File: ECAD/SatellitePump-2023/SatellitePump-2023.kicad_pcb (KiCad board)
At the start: 2 copper layers, 25 x 95 mm, 52 parts, among them J1 Conn_02x05_Odd_Even, J10 Conn_01x03, J11 Conn_01x03, J2 Conn_01x02, J3 Conn_01x03, J4 Conn_01x03, J5 Conn_01x03, J6 Conn_01x03, J7 CON_PUMP, J8 CON_EV, J9 Conn_01x03, Q1 AO3400A, Q2 AO3400A

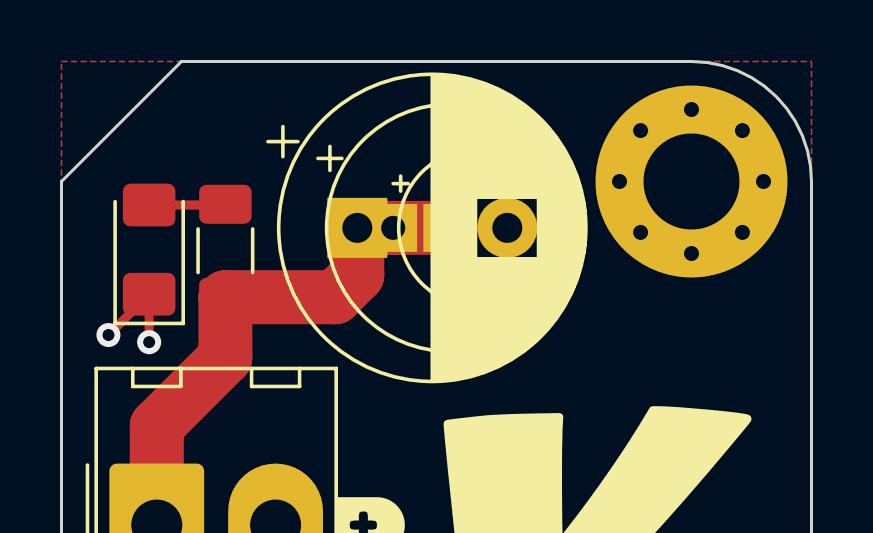
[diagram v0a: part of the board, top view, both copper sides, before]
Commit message: fix capacitor positions
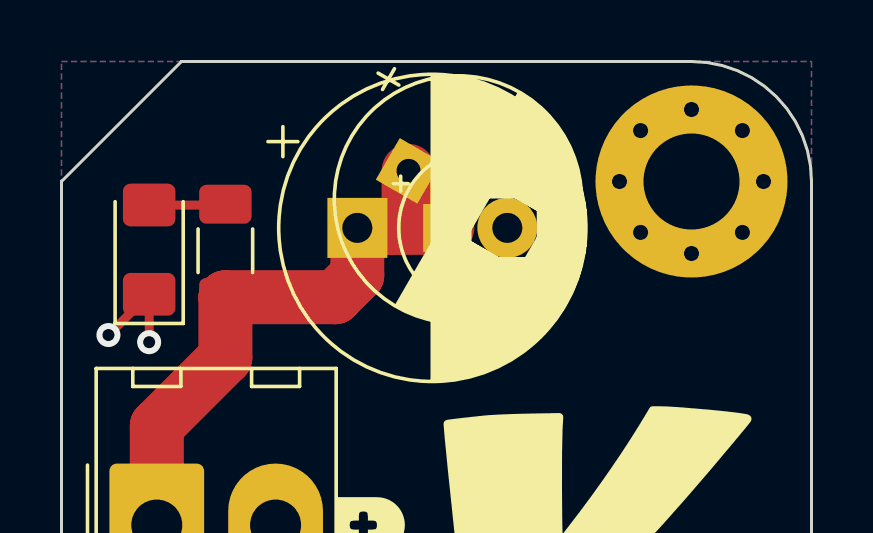
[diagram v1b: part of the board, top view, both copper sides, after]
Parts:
- moved C2 1.97 mm to (146.6, 48.6), turned to -30 degrees
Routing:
- net +5VP: track 125.0 -> 128.4 mm
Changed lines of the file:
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@@
   )
   (footprint "Capacitor_THT:CP_Radial_D8.0mm_P3.80mm" (layer "F.Cu")
-    (at 146.057349 50.546)
+    (at 146.569103 48.646 -30)
     (descr "CP, Radial series, Radial, pin pitch=3.80mm, , diameter=8mm, Electrolytic Capacitor")
     (tags "CP Radial series Radial pin pitch 3.80mm  diameter 8mm Electrolytic Capacitor")
@@
     (property "Sheetname" "")
     (attr through_hole)
-    (fp_text reference "C2" (at 1.9 -5.25) (layer "F.SilkS") hide
+    (fp_text reference "C2" (at 1.9 -5.25 150) (layer "F.SilkS") hide
       (effects (font (size 1 1) (thickness 0.15)))
     )
-    (fp_text value "C_Polarized_Small" (at 1.9 5.25) (layer "F.Fab")
+    (fp_text value "C_Polarized_Small" (at 1.9 5.25 150) (layer "F.Fab")
       (effects (font (size 1 1) (thickness 0.15)))
     )
-    (fp_text user "${REFERENCE}" (at 1.9 0) (layer "F.Fab")
+    (fp_text user "${REFERENCE}" (at 1.9 0 150) (layer "F.Fab")
       (effects (font (size 1 1) (thickness 0.15)))
     )
@@
     (fp_line (start -1.526759 -1.7475) (end -0.726759 -1.7475) (layer "F.Fab") (width 0.1))
     (fp_circle (center 1.9 0) (end 5.9 0) (layer "F.Fab") (width 0.1) (fill none))
-    (pad "1" thru_hole rect (at 0 0) (size 1.6 1.6) (drill 0.8) (layers *.Cu *.Mask)
+    (pad "1" thru_hole rect (at 0 0 330) (size 1.6 1.6) (drill 0.8) (layers *.Cu *.Mask)
       (net 1 "+5VP") (pintype "passive"))
-    (pad "2" thru_hole circle (at 3.8 0) (size 1.6 1.6) (drill 0.8) (layers *.Cu *.Mask)
+    (pad "2" thru_hole circle (at 3.8 0 330) (size 1.6 1.6) (drill 0.8) (layers *.Cu *.Mask)
       (net 2 "GND") (pintype "passive"))
     (model "${KIPRJMOD}/Packages3D/CP_Radial_D8.0mm_P3.80mm.wrl"
@@
   (segment (start 152.4 118.6275) (end 148.59 118.6275) (width 1.8) (layer "F.Cu") (net 1))
   (segment (start 145.287999 75.945999) (end 145.287999 70.003998) (width 1.8) (layer "F.Cu") (net 1))
+  (segment (start 144.86 50.546) (end 146.2024 50.546) (width 1.8) (layer "F.Cu") (net 1))
   (segment (start 140.462 52.858) (end 140.462 54.864) (width 1.8) (layer "F.Cu") (net 1))
   (segment (start 136.906 116.332) (end 139.2015 118.6275) (width 1.8) (layer "F.Cu") (net 1))
@@
   (segment (start 144.86 50.546) (end 146.057349 50.546) (width 1.8) (layer "F.Cu") (net 1))
   (segment (start 143.509999 118.6275) (end 146.049996 118.6275) (width 1.8) (layer "F.Cu") (net 1))
+  (segment (start 146.2024 50.546) (end 146.569103 50.179297) (width 1.8) (layer "F.Cu") (net 1))
   (segment (start 146.049996 118.6275) (end 146.049999 118.627497) (width 1.8) (layer "F.Cu") (net 1))
   (segment (start 138.176 65.278) (end 138.176 60.452) (width 1.8) (layer "F.Cu") (net 1))
@@
   (segment (start 145.287999 75.945999) (end 145.287999 79.248001) (width 1.8) (layer "F.Cu") (net 1))
   (segment (start 139.2015 118.6275) (end 143.509999 118.6275) (width 1.8) (layer "F.Cu") (net 1))
+  (segment (start 146.569103 50.179297) (end 146.569103 48.646) (width 1.8) (layer "F.Cu") (net 1))
   (segment (start 147.86 50.546) (end 146.057349 50.546) (width 1.8) (layer "F.Cu") (net 1))
   (segment (start 138.176 57.15) (end 138.176 60.452) (width 1.8) (layer "F.Cu") (net 1))
